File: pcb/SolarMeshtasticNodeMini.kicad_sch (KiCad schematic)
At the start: 31 parts, among them J2 Conn_01x02_Socket, J3 Conn_01x04_Socket, J4 Conn_01x02_Pin, J5 Conn_01x04_Socket, SW1 SSSS811101, SW2 SW_Push, U1 BQ25185, U2 HT-CT62, U3 HE9073A30MR, U4 APX803L05-32SA-7, U9 SS26_C5350986

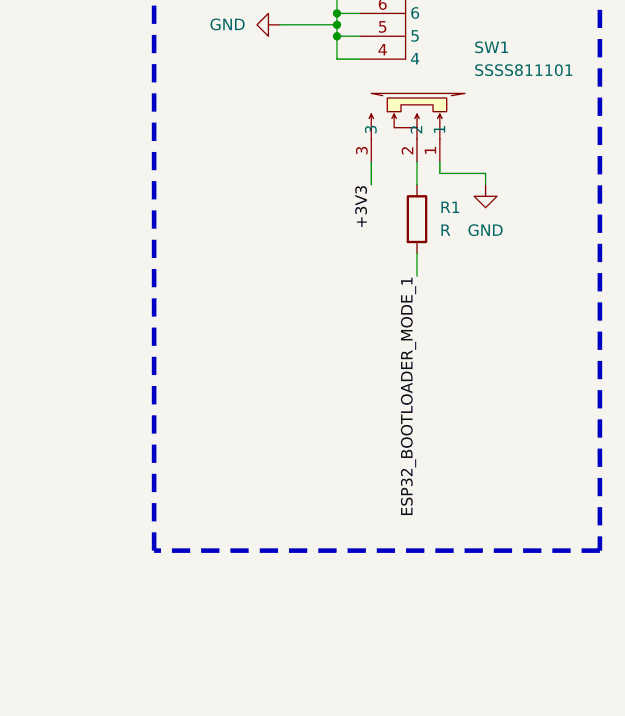
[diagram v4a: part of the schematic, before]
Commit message: pcb,sch: make the 3v3 of the bootloader switch weaker
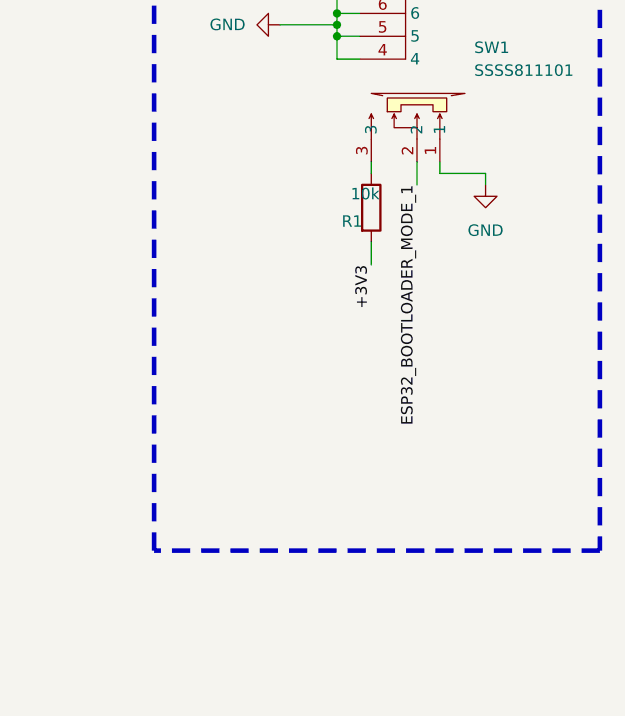
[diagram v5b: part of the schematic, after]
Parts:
- R1: value R -> 10k
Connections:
- net +3V3: now also R1.2; no longer SW1.3
- net ESP32_BOOTLOADER_MODE_1: now also SW1.2; no longer R1.2
- net at R1.1: now also SW1.3; no longer SW1.2
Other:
- moved on the sheet: R1
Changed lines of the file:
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@@
 	(wire
 		(pts
-			(xy 300.99 106.68) (xy 300.99 109.22)
+			(xy 20.32 156.21) (xy 22.86 156.21)
 		)
 		(stroke
@@
 	(wire
 		(pts
-			(xy 20.32 156.21) (xy 22.86 156.21)
+			(xy 123.19 166.37) (xy 123.19 171.45)
 		)
 		(stroke
@@
 	(wire
 		(pts
-			(xy 123.19 166.37) (xy 123.19 171.45)
+			(xy 50.8 55.88) (xy 34.29 55.88)
 		)
 		(stroke
@@
 	(wire
 		(pts
-			(xy 50.8 55.88) (xy 34.29 55.88)
+			(xy 88.9 62.23) (xy 88.9 63.5)
 		)
 		(stroke
@@
 	(wire
 		(pts
-			(xy 88.9 62.23) (xy 88.9 63.5)
+			(xy 22.86 137.16) (xy 22.86 138.43)
 		)
 		(stroke
@@
 	(wire
 		(pts
-			(xy 22.86 137.16) (xy 22.86 138.43)
+			(xy 25.4 45.72) (xy 50.8 45.72)
 		)
 		(stroke
@@
 	(wire
 		(pts
-			(xy 25.4 45.72) (xy 50.8 45.72)
+			(xy 20.32 137.16) (xy 22.86 137.16)
 		)
 		(stroke
@@
 	(wire
 		(pts
-			(xy 20.32 137.16) (xy 22.86 137.16)
+			(xy 295.91 105.41) (xy 295.91 107.95)
 		)
 		(stroke
@@
 	(wire
 		(pts
-			(xy 300.99 96.52) (xy 300.99 99.06)
+			(xy 218.44 96.52) (xy 228.6 96.52)
 		)
 		(stroke
@@
 	(wire
 		(pts
-			(xy 218.44 96.52) (xy 228.6 96.52)
+			(xy 25.4 33.02) (xy 25.4 35.56)
 		)
 		(stroke
@@
 	(wire
 		(pts
-			(xy 25.4 33.02) (xy 25.4 35.56)
+			(xy 83.82 123.19) (xy 83.82 130.81)
 		)
 		(stroke
@@
 	(wire
 		(pts
-			(xy 295.91 96.52) (xy 295.91 99.06)
+			(xy 25.4 156.21) (xy 29.21 156.21)
 		)
 		(stroke
@@
 	(wire
 		(pts
-			(xy 83.82 123.19) (xy 83.82 130.81)
+			(xy 76.2 135.89) (xy 77.47 135.89)
 		)
 		(stroke
@@
 	(wire
 		(pts
-			(xy 25.4 156.21) (xy 29.21 156.21)
+			(xy 147.32 39.37) (xy 147.32 41.91)
 		)
 		(stroke
@@
 	(wire
 		(pts
-			(xy 76.2 135.89) (xy 77.47 135.89)
+			(xy 295.91 96.52) (xy 295.91 97.79)
 		)
 		(stroke
@@
 	(wire
 		(pts
-			(xy 147.32 39.37) (xy 147.32 41.91)
+			(xy 127 209.55) (xy 127 214.63)
 		)
 		(stroke
@@
 	(wire
 		(pts
-			(xy 127 209.55) (xy 127 214.63)
+			(xy 125.73 132.08) (xy 121.92 132.08)
 		)
 		(stroke
@@
 	(wire
 		(pts
-			(xy 125.73 132.08) (xy 121.92 132.08)
+			(xy 180.34 83.82) (xy 182.88 83.82)
 		)
 		(stroke
@@
 	(wire
 		(pts
-			(xy 180.34 83.82) (xy 182.88 83.82)
+			(xy 55.88 140.97) (xy 55.88 142.24)
 		)
 		(stroke
@@
 	(wire
 		(pts
-			(xy 55.88 140.97) (xy 55.88 142.24)
+			(xy 120.65 80.01) (xy 120.65 85.09)
 		)
 		(stroke
@@
 	(wire
 		(pts
-			(xy 120.65 80.01) (xy 120.65 85.09)
+			(xy 300.99 96.52) (xy 300.99 99.06)
 		)
 		(stroke
@@
 	)
 	(label "+3V3"
-		(at 295.91 99.06 270)
+		(at 295.91 107.95 270)
 		(effects
 			(font
@@
 	)
 	(label "ESP32_BOOTLOADER_MODE_1"
-		(at 300.99 109.22 270)
+		(at 300.99 99.06 270)
 		(effects
 			(font
@@
 	(symbol
 		(lib_id "Device:R")
-		(at 300.99 102.87 0)
+		(at 295.91 101.6 0)
 		(unit 1)
 		(exclude_from_sim no)
@@
 		(on_board yes)
 		(dnp no)
-		(fields_autoplaced yes)
 		(property "Reference" "R1"
-			(at 303.53 101.5999 0)
+			(at 292.608 103.124 0)
 			(effects
 				(font
@@
 			)
 		)
-		(property "Value" "R"
-			(at 303.53 104.1399 0)
+		(property "Value" "10k"
+			(at 293.624 100.076 0)
 			(effects
 				(font
@@
 		)
 		(property "Footprint" "Resistor_SMD:R_0805_2012Metric_Pad1.20x1.40mm_HandSolder"
-			(at 299.212 102.87 90)
+			(at 294.132 101.6 90)
 			(effects
 				(font
@@
 		)
 		(property "Datasheet" "~"
-			(at 300.99 102.87 0)
+			(at 295.91 101.6 0)
 			(effects
 				(font
@@
 		)
 		(property "Description" "Resistor"
-			(at 300.99 102.87 0)
+			(at 295.91 101.6 0)
 			(effects
 				(font

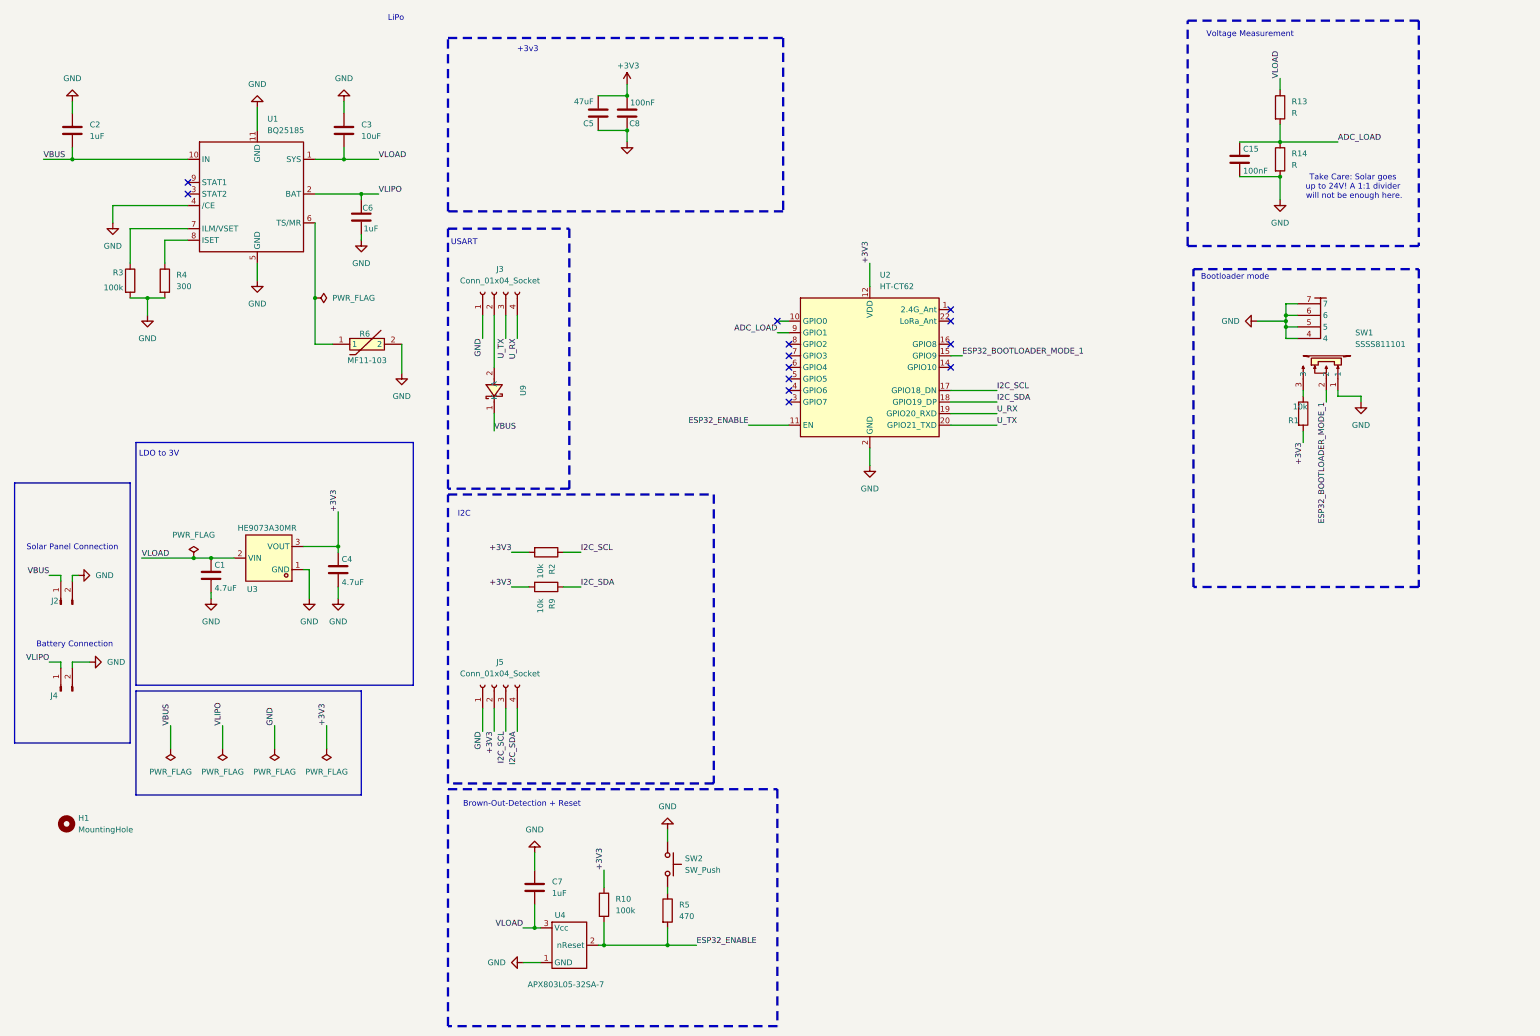
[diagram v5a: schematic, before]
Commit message: pcb, sch: add load switch to control entire 3.3V rail
Until now only the ESP32 was disabled if the voltage drops due to
discharge. This might cause the sensors to slip into a slow brown-out.
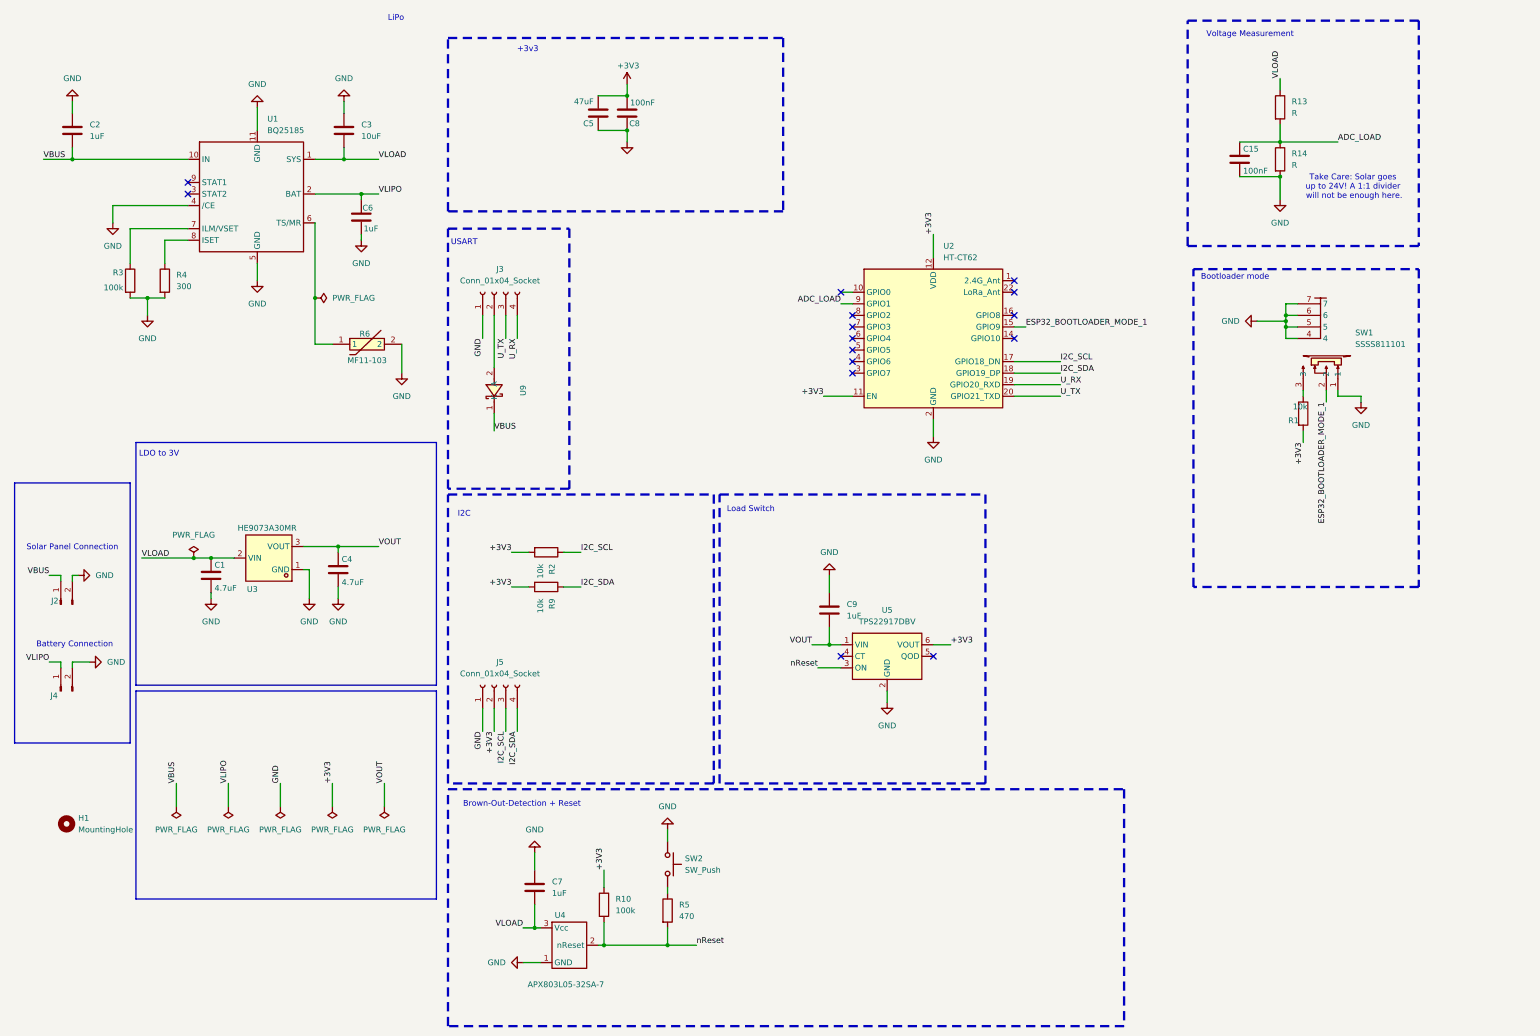
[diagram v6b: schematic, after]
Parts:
- added C9: 1uF, Capacitor_SMD:C_0805_2012Metric_Pad1.18x1.45mm_HandSolder, symbol Device:C
- added U5: TPS22917DBV, Package_TO_SOT_SMD:SOT-23-6, symbol Power_Management:TPS22917DBV
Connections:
- net +3V3: now also U2.11 (EN), U5.6 (VOUT); no longer C4.1, U3.3 (VOUT)
- net GND: now also C9.2, U5.2 (GND)
- net ESP32_ENABLE renamed nReset
- net nReset: now also U5.3 (ON); no longer U2.11 (EN)
- new net VOUT: C4.1, C9.1, U3.3 (VOUT), U5.1 (VIN)
- no-connect marks 13 -> 15
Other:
- note added: "Load Switch"
- moved on the sheet: U2
